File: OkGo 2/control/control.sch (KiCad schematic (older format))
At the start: 40 parts

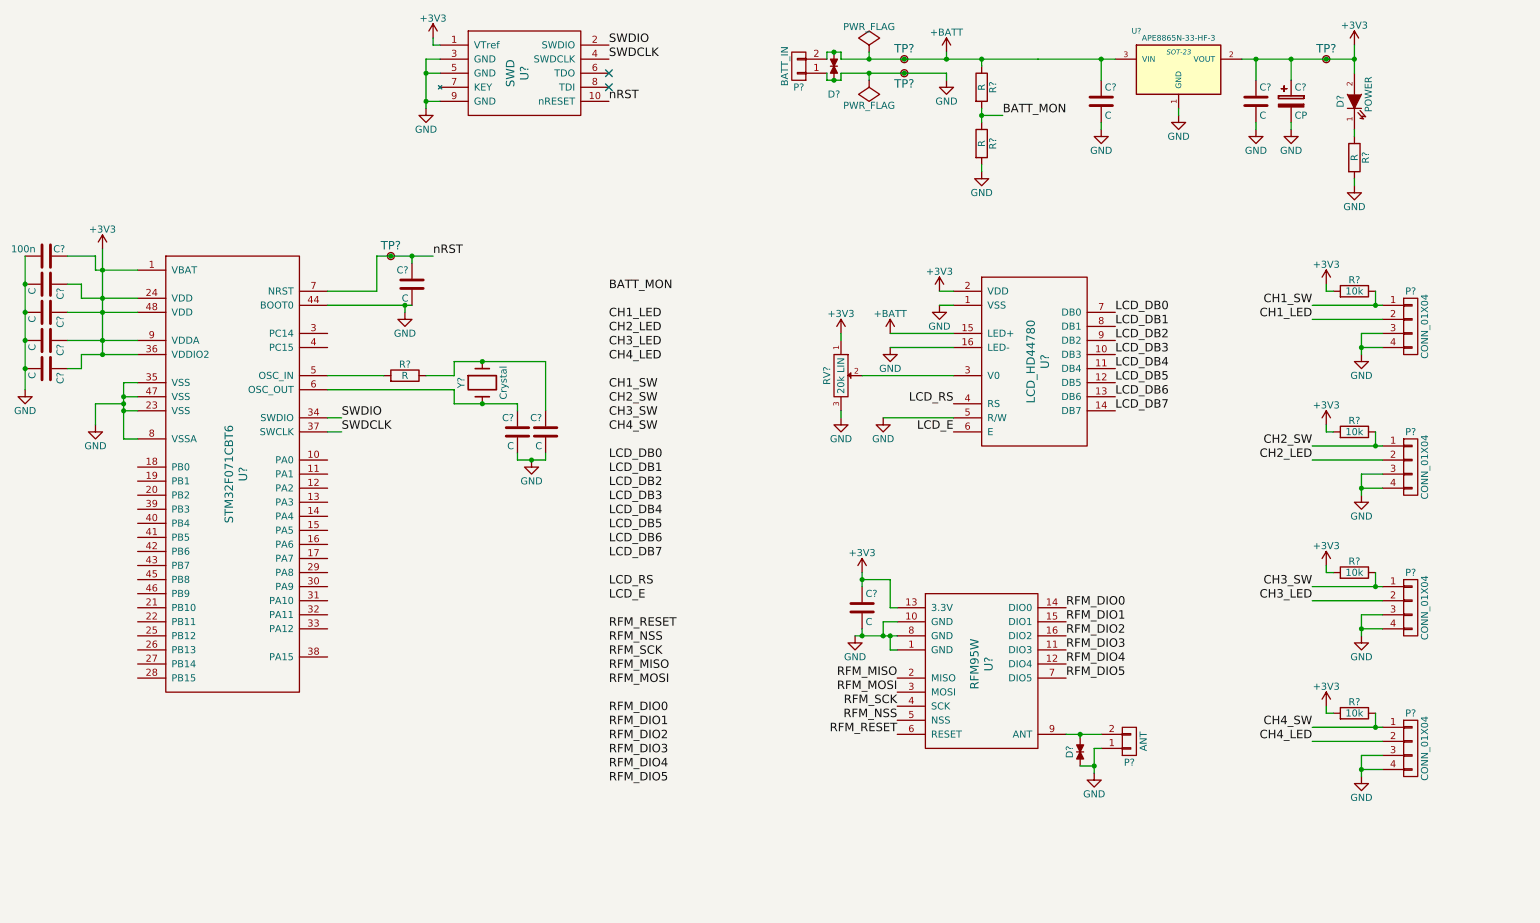
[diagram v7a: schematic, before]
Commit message: Moved xtal drive resistors. Fixes #15
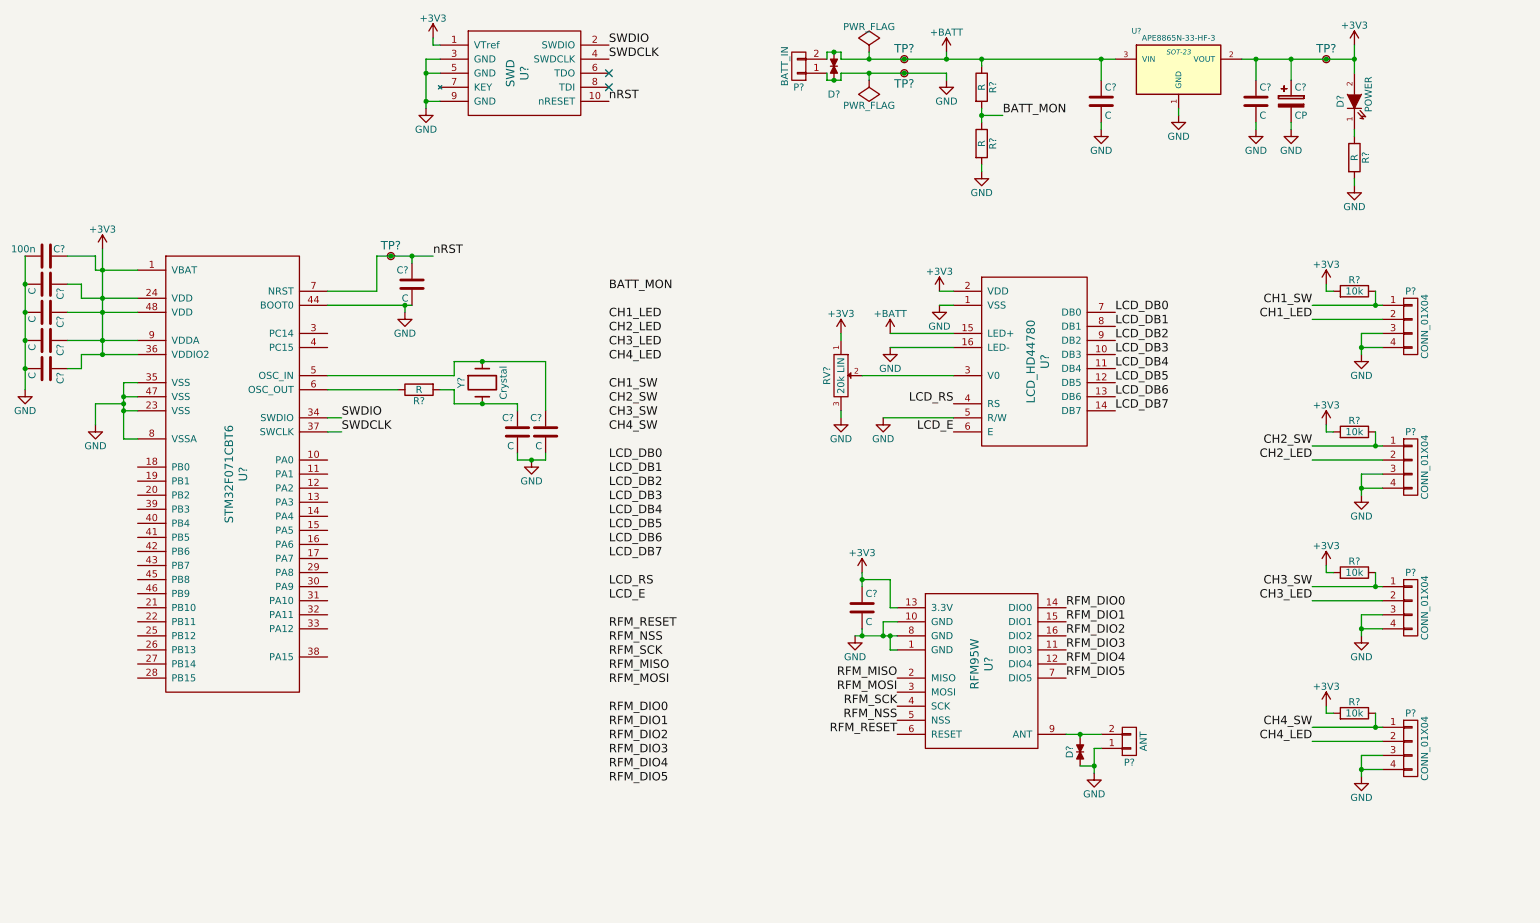
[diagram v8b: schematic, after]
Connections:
- net at C?.1, Y?.1: now also U?.5 (OSC_IN); no longer R?.1
- net at C?.1, Y?.2: now also R?.2; no longer U?.6 (OSC_OUT)
- new net: R?.1, U?.6 (OSC_OUT)
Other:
- moved on the sheet: R?
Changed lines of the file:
@@
 L R R?
 U 1 1 5563219C
-P 3550 3350
-F 0 "R?" V 3630 3350 50  0000 C CNN
-F 1 "R" V 3550 3350 50  0000 C CNN
-F 2 "" V 3480 3350 30  0000 C CNN
-F 3 "" H 3550 3350 30  0000 C CNN
-	1    3550 3350
-	0    1    -1   0
+P 3650 3450
+F 0 "R?" V 3730 3450 50  0000 C CNN
+F 1 "R" V 3650 3450 50  0000 C CNN
+F 2 "" V 3580 3450 30  0000 C CNN
+F 3 "" H 3650 3450 30  0000 C CNN
+	1    3650 3450
+	0    -1   1    0
 $EndComp
 $Comp
@@
 	9850 1550 9850 1600
 Wire Wire Line
-	9500 1100 9600 1100
-Wire Wire Line
-	9600 1100 9850 1100
-Wire Wire Line
-	9850 1100 10100 1100
-Wire Wire Line
-	10100 1100 10300 1100
+	9500 1100 10300 1100
 Wire Wire Line
 	9600 1100 9600 1250
@@
 Connection ~ 9600 1100
 Wire Wire Line
-	10300 1000 10300 1100
-Wire Wire Line
-	10300 1100 10300 1200
+	10300 1000 10300 1200
 Connection ~ 9850 1100
 Wire Wire Line
-	6650 1200 6850 1200
-Wire Wire Line
-	6850 1200 7400 1200
+	6650 1200 7400 1200
 Wire Wire Line
 	6850 1050 6850 1100
@@
 	10350 3150 10500 3150
 Wire Wire Line
-	10350 3050 10350 3150
-Wire Wire Line
-	10350 3150 10350 3200
+	10350 3050 10350 3200
 Wire Wire Line
 	10450 2850 10450 2750
@@
 	8500 6000 8450 6000
 Wire Wire Line
-	8450 6000 8450 6125
-Wire Wire Line
-	8450 6125 8450 6175
-Wire Wire Line
-	6750 5200 6800 5200
-Wire Wire Line
-	6800 5200 6950 5200
-Wire Wire Line
-	6950 5200 7000 5200
-Wire Wire Line
-	7000 5200 7050 5200
+	8450 6000 8450 6175
+Wire Wire Line
+	6750 5200 7050 5200
 Wire Wire Line
 	7000 5200 7000 5300
@@
 Connection ~ 6950 5200
 Wire Wire Line
-	6800 4750 6800 4800
-Wire Wire Line
-	6800 4800 6800 4850
+	6800 4750 6800 4850
 Wire Wire Line
 	6800 4800 7000 4800
@@
 Connection ~ 6800 5200
 Wire Wire Line
-	8250 5900 8350 5900
-Wire Wire Line
-	8350 5900 8500 5900
-Wire Wire Line
-	1400 2450 1400 2600
-Wire Wire Line
-	1400 2600 1400 2800
-Wire Wire Line
-	1400 2800 1400 2900
-Wire Wire Line
-	1400 2900 1400 3100
-Wire Wire Line
-	1400 3100 1400 3200
-Wire Wire Line
-	1250 2800 1400 2800
-Wire Wire Line
-	1400 2800 1650 2800
-Wire Wire Line
-	1150 2900 1400 2900
-Wire Wire Line
-	1400 2900 1650 2900
+	8250 5900 8500 5900
+Wire Wire Line
+	1400 2450 1400 3200
+Wire Wire Line
+	1250 2800 1650 2800
+Wire Wire Line
+	1150 2900 1650 2900
 Connection ~ 1400 2800
 Wire Wire Line
-	1150 3100 1400 3100
-Wire Wire Line
-	1400 3100 1650 3100
+	1150 3100 1650 3100
 Connection ~ 1400 2900
 Wire Wire Line
-	1250 3200 1400 3200
-Wire Wire Line
-	1400 3200 1650 3200
+	1250 3200 1650 3200
 Connection ~ 1400 3100
 Connection ~ 1400 3200
@@
 	1650 3400 1550 3400
 Wire Wire Line
-	1550 3400 1550 3500
-Wire Wire Line
-	1550 3500 1550 3550
-Wire Wire Line
-	1550 3550 1550 3600
-Wire Wire Line
-	1550 3600 1550 3800
+	1550 3400 1550 3800
 Wire Wire Line
 	1550 3500 1650 3500
@@
 Connection ~ 3600 2500
 Wire Wire Line
-	3000 2850 3550 2850
-Wire Wire Line
-	3550 2850 3600 2850
+	3000 2850 3600 2850
 Wire Wire Line
 	3550 2850 3550 2900
 Wire Wire Line
-	3350 2500 3600 2500
-Wire Wire Line
-	3600 2500 3750 2500
+	3350 2500 3750 2500
 Wire Wire Line
 	3350 2750 3000 2750
 Wire Wire Line
-	3700 3350 3900 3350
+	3000 3350 3900 3350
 Wire Wire Line
 	3900 3350 3900 3250
 Wire Wire Line
-	3900 3250 4100 3250
-Wire Wire Line
-	4100 3250 4550 3250
+	3900 3250 4550 3250
 Wire Wire Line
 	3900 3450 3900 3550
 Wire Wire Line
-	3900 3550 4100 3550
-Wire Wire Line
-	4100 3550 4350 3550
+	3900 3550 4350 3550
 Wire Wire Line
 	4350 3550 4350 3600
@@
 	4550 3950 4550 3900
 Wire Wire Line
-	4350 3950 4450 3950
-Wire Wire Line
-	4450 3950 4550 3950
+	4350 3950 4550 3950
 Connection ~ 4450 3950
 Wire Wire Line
@@
 	1250 3300 1150 3300
 Wire Wire Line
-	850  2500 850  2700
-Wire Wire Line
-	850  2700 850  2900
-Wire Wire Line
-	850  2900 850  3100
-Wire Wire Line
-	850  3100 850  3300
-Wire Wire Line
-	850  3300 850  3450
+	850  2500 850  3450
 Connection ~ 850  2900
 Connection ~ 850  3100
@@
 	3800 1100 3700 1100
 Wire Wire Line
-	3700 1100 3700 1200
-Wire Wire Line
-	3700 1200 3700 1400
-Wire Wire Line
-	3700 1400 3700 1450
+	3700 1100 3700 1450
 Wire Wire Line
 	3700 1400 3800 1400
@@
 	1350 2500 1350 2600
 Wire Wire Line
-	1350 2600 1400 2600
-Wire Wire Line
-	1400 2600 1650 2600
+	1350 2600 1650 2600
 Connection ~ 1400 2600
 Connection ~ 850  2700
@@
 	7650 1850 7650 1900
 Wire Wire Line
-	7650 1450 7650 1500
-Wire Wire Line
-	7650 1500 7650 1550
+	7650 1450 7650 1550
 Wire Wire Line
 	7650 1500 7800 1500
 Connection ~ 7650 1500
 Wire Wire Line
-	6650 1100 6850 1100
-Wire Wire Line
-	6850 1100 7400 1100
-Wire Wire Line
-	7400 1100 7650 1100
-Wire Wire Line
-	7650 1100 8050 1100
-Wire Wire Line
-	8050 1100 8500 1100
-Wire Wire Line
-	8500 1100 8600 1100
+	6650 1100 8600 1100
 $Comp
 L LCD_HD44780 U?
@@
 	3350 2500 3350 2750
 Connection ~ 3550 2850
-Wire Wire Line
-	3000 3350 3400 3350
-Wire Wire Line
-	3000 3450 3900 3450
 $Comp
 L TVS_small D?
@@
 	6550 1100 6550 1050
 Wire Wire Line
-	6550 1050 6600 1050
-Wire Wire Line
-	6600 1050 6650 1050
+	6550 1050 6650 1050
 Wire Wire Line
 	6600 1050 6600 1050
@@
 	6550 1200 6550 1250
 Wire Wire Line
-	6550 1250 6600 1250
-Wire Wire Line
-	6600 1250 6650 1250
+	6550 1250 6650 1250
 Wire Wire Line
 	6600 1250 6600 1250
@@
 BATT_MON
 Wire Wire Line
-	10000 2850 10450 2850
-Wire Wire Line
-	10450 2850 10500 2850
+	10000 2850 10500 2850
 Text Label 10000 2850 2    60   ~ 0
 CH1_SW
@@
 	10350 4150 10500 4150
 Wire Wire Line
-	10350 4050 10350 4150
-Wire Wire Line
-	10350 4150 10350 4200
+	10350 4050 10350 4200
 Wire Wire Line
 	10450 3850 10450 3750
@@
 Connection ~ 10350 4150
 Wire Wire Line
-	10000 3850 10450 3850
-Wire Wire Line
-	10450 3850 10500 3850
+	10000 3850 10500 3850
 Text Label 10000 3850 2    60   ~ 0
 CH2_SW
@@
 	10350 5150 10500 5150
 Wire Wire Line
-	10350 5050 10350 5150
-Wire Wire Line
-	10350 5150 10350 5200
+	10350 5050 10350 5200
 Wire Wire Line
 	10450 4850 10450 4750
@@
 Connection ~ 10350 5150
 Wire Wire Line
-	10000 4850 10450 4850
-Wire Wire Line
-	10450 4850 10500 4850
+	10000 4850 10500 4850
 Text Label 10000 4850 2    60   ~ 0
 CH3_SW
@@
 	10350 6150 10500 6150
 Wire Wire Line
-	10350 6050 10350 6150
-Wire Wire Line
-	10350 6150 10350 6200
+	10350 6050 10350 6200
 Wire Wire Line
 	10450 5850 10450 5750
@@
 Connection ~ 10350 6150
 Wire Wire Line
-	10000 5850 10450 5850
-Wire Wire Line
-	10450 5850 10500 5850
+	10000 5850 10500 5850
 Text Label 10000 5850 2    60   ~ 0
 CH4_SW
@@
 $EndComp
 Connection ~ 3450 2500
+Wire Wire Line
+	3000 3450 3500 3450
+Wire Wire Line
+	3800 3450 3900 3450
 $EndSCHEMATC
